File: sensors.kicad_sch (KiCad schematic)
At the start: 19 parts, among them CN2 SM04B-SRSS-TB (LF)(SN), CN3 SM04B-SRSS-TB (LF)(SN), U4 OPT3004DNPR, U7 ICM-42688-P, U8 BME280, U9 SN74AHCT1G125DBVR

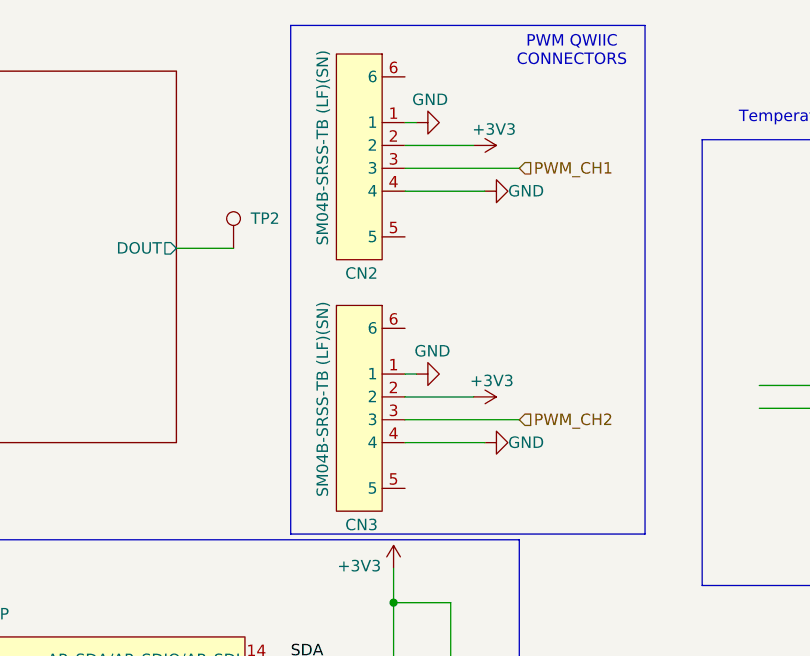
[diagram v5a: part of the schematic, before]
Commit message: replaced part for lower cost
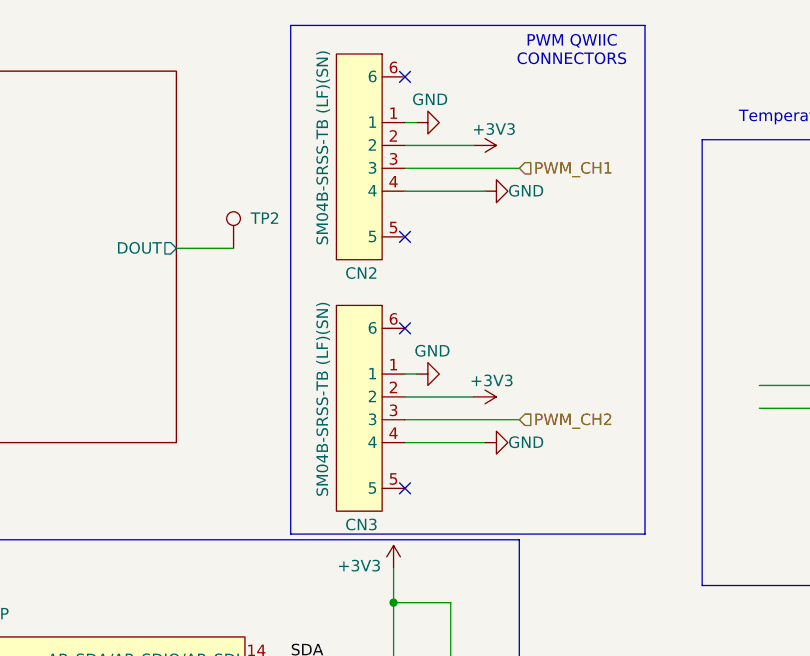
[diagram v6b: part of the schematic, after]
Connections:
- no-connect marks 6 -> 10
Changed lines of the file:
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@@
+	)
+	(no_connect
+		(at 137.16 19.05)
 	)
 	(no_connect
@@
 	)
 	(no_connect
+		(at 137.16 64.77)
+	)
+	(no_connect
 		(at 62.23 172.72)
+	)
+	(no_connect
+		(at 137.16 36.83)
 	)
 	(no_connect
@@
 	)
 	(no_connect
+		(at 137.16 46.99)
+	)
+	(no_connect

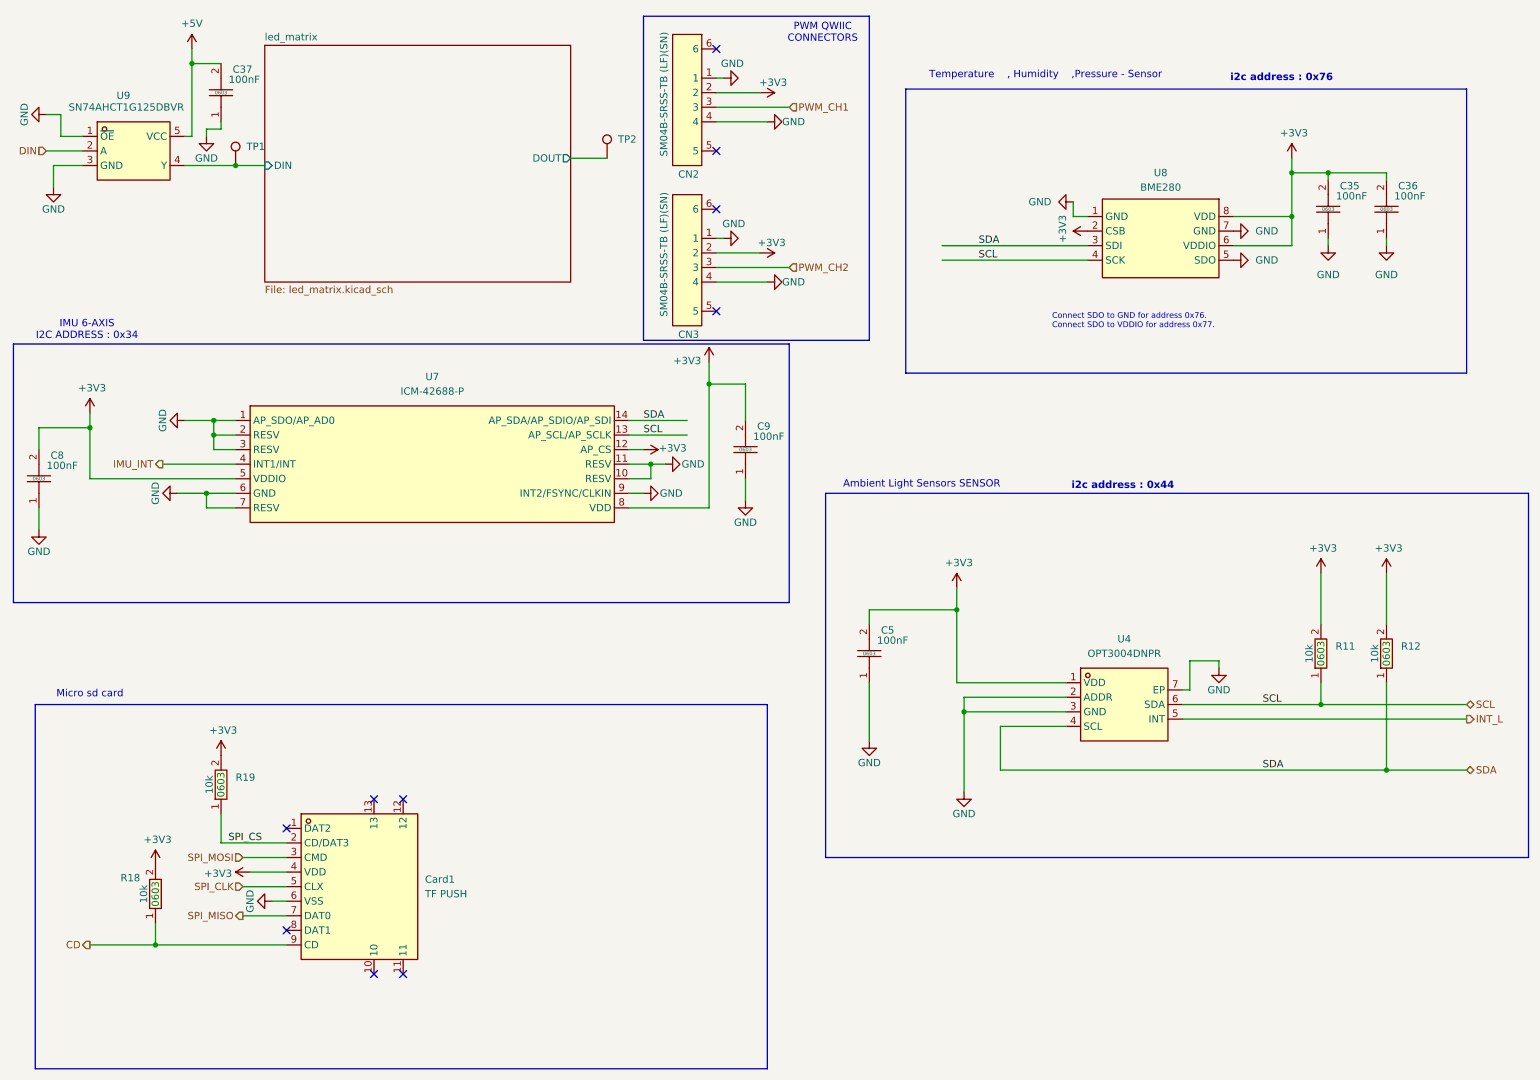
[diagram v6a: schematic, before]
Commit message: Changed lga sensors to cheap qfn soic8 package
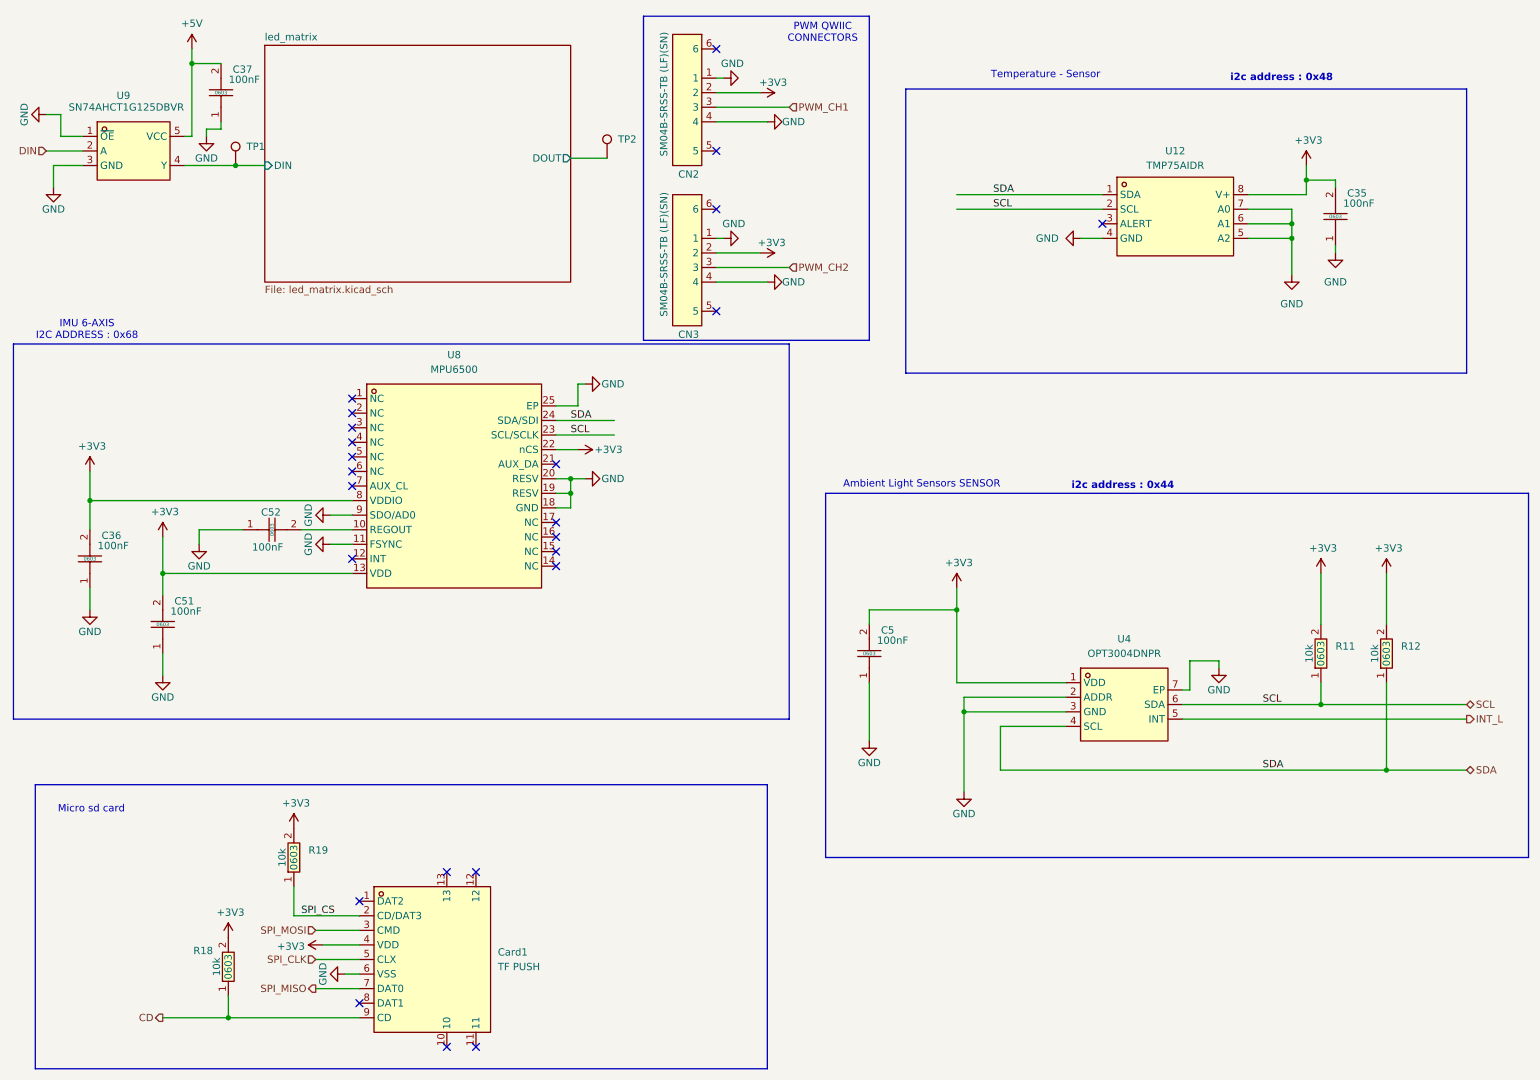
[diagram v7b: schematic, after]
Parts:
- removed C8, C9: CC0603KRX7R9BB104, easyeda2kicad:C0603, symbol easyeda2kicad:CC0603KRX7R9BB104
- removed U7: ICM-42688-P, easyeda2kicad:LGA-14_L3.0-W2.5-P0.50-TL, symbol easyeda2kicad:ICM-42688-P
- removed U8: BME280, easyeda2kicad:LGA-8_BME280_BL, symbol easyeda2kicad:BME280
- added C51, C52: CC0603KRX7R9BB104, easyeda2kicad:C0603, symbol easyeda2kicad:CC0603KRX7R9BB104
- added U12: TMP75AIDR, easyeda2kicad:SOIC-8_L4.9-W3.9-P1.27-LS6.0-BL, symbol easyeda_symbole:TMP75AIDR
- added U8: MPU6500, easyeda2kicad:QFN-24_L3.0-W3.0-P0.40-BL-EP, symbol easyeda_symbole:MPU6500
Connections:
- net +3V3: now also C51.2, U12.8 (V+), U8.13 (VDD), U8.22 (nCS), U8.8 (VDDIO)
- net GND: now also C51.1, C52.1, U12.4 (GND), U12.5 (A2), U12.6 (A1), U12.7 (A0), U8.11 (FSYNC), U8.18 (GND), U8.19 (RESV), U8.20 (RESV), U8.25 (EP), U8.9 (SDO/AD0)
- net SCL: now also U12.2 (SCL), U8.23 (SCL/SCLK)
- net SDA: now also U12.1 (SDA), U8.24 (SDA/SDI)
- new net: C52.2, U8.10 (REGOUT)
- no-connect marks 10 -> 24
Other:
- note added: "IMU 6-AXIS I2C ADDRESS : 0x68"
- note added: "Temperature - Sensor"
- note added: "i2c address : 0x48"
- note removed: "IMU 6-AXIS I2C ADDRESS : 0x34"
- note removed: "Temperature , Humidity ,Pressure - Sensor"
- note removed: "i2c address : 0x76"
- moved on the sheet: C35, Card1, R18, R19

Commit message: Changed a bit component that where out of stock
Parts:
- removed Card1: TF PUSH, easyeda2kicad:TF-SMD_TF-PUSH, symbol easyeda2kicad:TFPUSH
- added Card1: TF PUSH, easyeda2kicad:TF-SMD_TF-PUSH, symbol easyeda_symbole:TFPUSH
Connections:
- net +3V3: now also Card1.4 (VDD)
- net CD: now also Card1.9 (CD)
- net GND: now also Card1.6 (VSS)
- net SPI_CLK: now also Card1.5 (CLX)
- net SPI_CS: now also Card1.2 (CD/DAT3)
- net SPI_MISO: now also Card1.7 (DAT0)
- net SPI_MOSI: now also Card1.3 (CMD)
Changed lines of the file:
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@@
+	)
+	(symbol
+		(lib_id "easyeda_symbole:TFPUSH")
+		(at 85.09 177.8 0)
+		(unit 1)
+		(exclude_from_sim no)
+		(in_bom yes)
+		(on_board yes)
+		(dnp no)
+		(fields_autoplaced yes)
+		(property "Reference" "Card1"
+			(at 99.06 176.5299 0)
+			(effects
+				(font
+					(size 1.27 1.27)
+				)
+				(justify left)
+			)
+		)
+		(property "Value" "TF PUSH"
+			(at 99.06 179.0699 0)
+			(effects
+				(font
+					(size 1.27 1.27)
+				)
+				(justify left)
+			)
+		)
+		(property "Footprint" "easyeda2kicad:TF-SMD_TF-PUSH"
+			(at 85.09 200.66 0)
+			(effects
+				(font
+					(size 1.27 1.27)
+				)
+				(hide yes)
+			)
+		)
+		(property "Datasheet" "https://lcsc.com/product-detail/Connector-Card-Sockets_SHOU-HAN-SHOU-HAN-TFDeck-TF-Deck_C393941.html"
+			(at 85.09 203.2 0)
+			(effects
+				(font
+					(size 1.27 1.27)
+				)
+				(hide yes)
+			)
+		)
+		(property "Description" ""
+			(at 85.09 177.8 0)
+			(effects
+				(font
+					(size 1.27 1.27)
+				)
+				(hide yes)
+			)
+		)
+		(property "LCSC Part" "C393941"
+			(at 85.09 205.74 0)
+			(effects
+				(font
+					(size 1.27 1.27)
+				)
+				(hide yes)
+			)
+		)
+		(pin "1"
+		)
+		(pin "12"
+		)
+		(pin "9"
+		)
+		(pin "3"
+		)
+		(pin "4"
+		)
+		(pin "13"
+		)
+		(pin "10"
+		)
+		(pin "6"
+		)
+		(pin "5"
+		)
+		(pin "8"
+		)
+		(pin "11"
+		)
+		(pin "7"
+		)
+		(pin "2"
+		)
+		(instances
+			(project ""
+				(path "/6657db5f-e034-448d-bae3-f44b9f033a3a/11458ec3-e8ed-4a92-914f-257f2d6c1b04"
+					(reference "Card1")
+					(unit 1)
+				)
+			)
+		)
 	)
 	(symbol
@@
 					(unit 1)
 				)
-			)
-		)
-	)
-	(symbol
-		(lib_id "easyeda2kicad:TFPUSH")
-		(at 85.09 177.8 0)
-		(unit 1)
-		(exclude_from_sim no)
-		(in_bom yes)
-		(on_board yes)
-		(dnp no)
-		(fields_autoplaced yes)
-		(property "Reference" "Card1"
-			(at 99.06 176.5299 0)
-			(effects
-				(font
-					(size 1.27 1.27)
-				)
-				(justify left)
-			)
-		)
-		(property "Value" "TF PUSH"
-			(at 99.06 179.0699 0)
-			(effects
-				(font
-					(size 1.27 1.27)
-				)
-				(justify left)
-			)
-		)
-		(property "Footprint" "easyeda2kicad:TF-SMD_TF-PUSH"
-			(at 85.09 200.66 0)
-			(effects
-				(font
-					(size 1.27 1.27)
-				)
-				(hide yes)
-			)
-		)
-		(property "Datasheet" "https://lcsc.com/product-detail/Connector-Card-Sockets_SHOU-HAN-SHOU-HAN-TFDeck-TF-Deck_C393941.html"
-			(at 85.09 203.2 0)
-			(effects
-				(font
-					(size 1.27 1.27)
-				)
-				(hide yes)
-			)
-		)
-		(property "Description" ""
-			(at 85.09 177.8 0)
-			(effects
-				(font
-					(size 1.27 1.27)
-				)
-				(hide yes)
-			)
-		)
-		(property "LCSC Part" "C393941"
-			(at 85.09 205.74 0)
-			(effects
-				(font
-					(size 1.27 1.27)
-				)
-				(hide yes)
-			)
-		)
-		(pin "1"
-		)
-		(pin "11"
-		)
-		(pin "8"
-		)
-		(pin "12"
-		)
-		(pin "2"
-		)
-		(pin "5"
-		)
-		(pin "7"
-		)
-		(pin "6"
-		)
-		(pin "13"
-		)
-		(pin "4"
-		)
-		(pin "9"
-		)
-		(pin "3"
-		)
-		(pin "10"
-		)
-		(instances
-			(project ""
-				(path "/6657db5f-e034-448d-bae3-f44b9f033a3a/11458ec3-e8ed-4a92-914f-257f2d6c1b04"
-					(reference "Card1")
-					(unit 1)
-				)
